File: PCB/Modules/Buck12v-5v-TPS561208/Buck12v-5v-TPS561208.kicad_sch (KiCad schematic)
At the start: 8 parts, among them U1 TPS561208DDCT

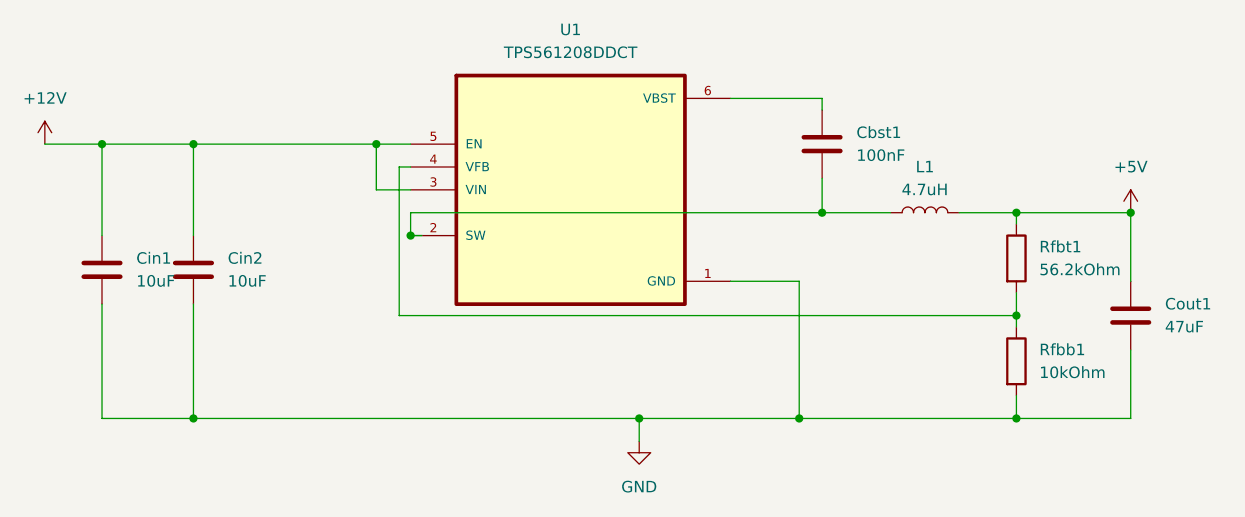
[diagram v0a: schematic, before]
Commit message: Added buck design
Signed-off-by: Simonca Raul <simonca.raul@gmail.com>
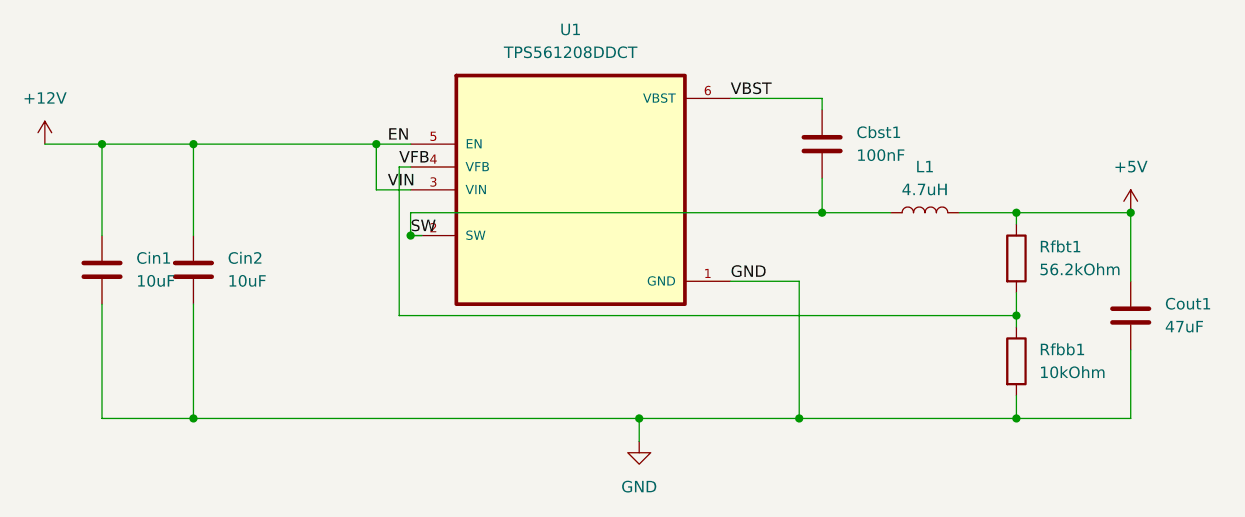
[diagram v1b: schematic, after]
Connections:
- net SW: now reaches Cbst1.2, L1.1, U1.2 (SW)
- net VFB: now reaches Rfbb1.1, Rfbt1.2, U1.4 (VFB)
- net VBST: now reaches Cbst1.1, U1.6 (VBST)
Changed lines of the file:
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@@
+		)
+	)
+	(label "GND"
+		(at 168.91 99.06 0)
+		(fields_autoplaced yes)
+		(effects
+			(font
+				(size 1.27 1.27)
+			)
+			(justify left bottom)
+		)
+	)
+	(label "SW"
+		(at 133.35 93.98 0)
+		(fields_autoplaced yes)
+		(effects
+			(font
+				(size 1.27 1.27)
+			)
+			(justify left bottom)
+		)
+	)
+	(label "VFB"
+		(at 132.08 86.36 0)
+		(fields_autoplaced yes)
+		(effects
+			(font
+				(size 1.27 1.27)
+			)
+			(justify left bottom)
+		)
+	)
+	(label "VIN"
+		(at 130.81 88.9 0)
+		(fields_autoplaced yes)
+		(effects
+			(font
+				(size 1.27 1.27)
+			)
+			(justify left bottom)
+		)
+	)
+	(label "VBST"
+		(at 168.91 78.74 0)
+		(fields_autoplaced yes)
+		(effects
+			(font
+				(size 1.27 1.27)
+			)
+			(justify left bottom)
+		)
+	)
+	(label "EN"
+		(at 130.81 83.82 0)
+		(fields_autoplaced yes)
+		(effects
+			(font
+				(size 1.27 1.27)
+			)
+			(justify left bottom)
 		)
 	)
